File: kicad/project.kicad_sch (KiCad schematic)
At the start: 15 parts, among them IC1A Conn_02x08_Counter_Clockwise, IC1B Conn_02x08_Counter_Clockwise, Q1 AO3402, Q2 AO3401, SW1 RotaryEncoder_Switch, U2 I2C 0.91 OLED

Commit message: Updating the schematic with footprint and symbol
Tiny weaks to pin assignment
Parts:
- removed IC1A, IC1B: Conn_02x08_Counter_Clockwise, symbol Connector_Generic:Conn_02x08_Counter_Clockwise
- added U1: WEMOS_ESP32_S2_Mini, library:WEMOS_S2_mini, symbol library:WEMOS_ESP32_S2_Mini
- BT1: footprint (none) -> Connector_PinHeader_2.54mm:PinHeader_1x02_P2.54mm_Vertical
- R1, R2, R3, R4, R5, R6, R7: footprint (none) -> Resistor_THT:R_Axial_DIN0207_L6.3mm_D2.5mm_P10.16mm_Horizontal
- U2: value I2C 0.91 OLED -> I2C 0.91 128x32 OLED
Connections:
- net +BATT: now also U1.47 (VBUS)
- net BAT_SENSE: now also U1.17 (GPIO17)
- net DISPLAY_PWR: now also U1.37 (GPIO37)
- net ENC1: now also U1.18 (GPIO18)
- net ENC2: now also U1.21 (GPIO21)
- net ENC_BTN: now also U1.16 (GPIO16)
- net GND: now also U1.48 (GND)
- net IR_LED: now also U1.15 (GPIO15)
- net SCL: now also U1.35 (GPIO35)
- net SDA: now also U1.33 (GPIO33)
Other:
- note removed: "I^{2}C OLED DISPLAY 128x32"
- note removed: "WEMOS ESP32-S2-mini"
- moved on the sheet: BT1, D1, Q1, Q2, R1, R2, R3, R4, R5, R6, R7, SW1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

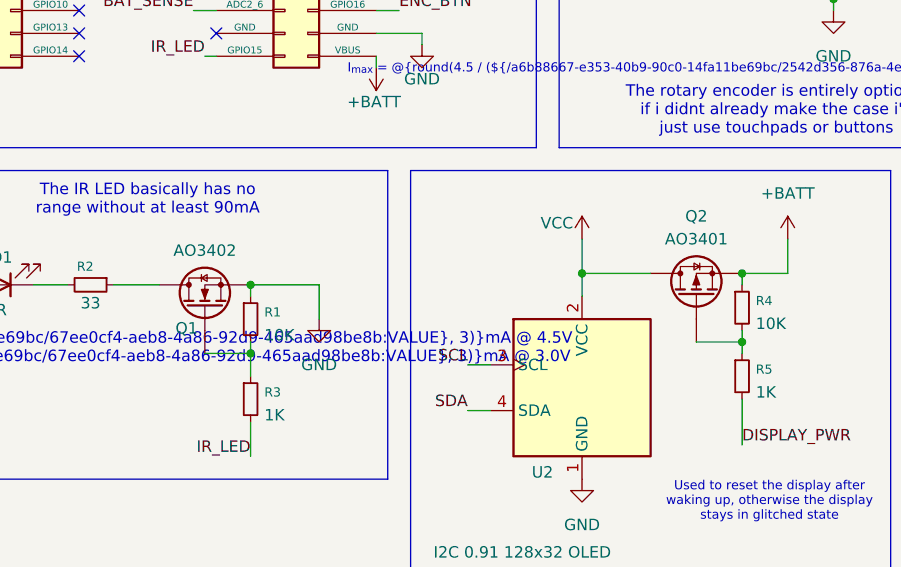
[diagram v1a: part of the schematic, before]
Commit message: Update schematic to show proper pinout of mosfets
As i am soldering this without making a PCB it is very helpful so i dont
have to look at the datasheet all the time
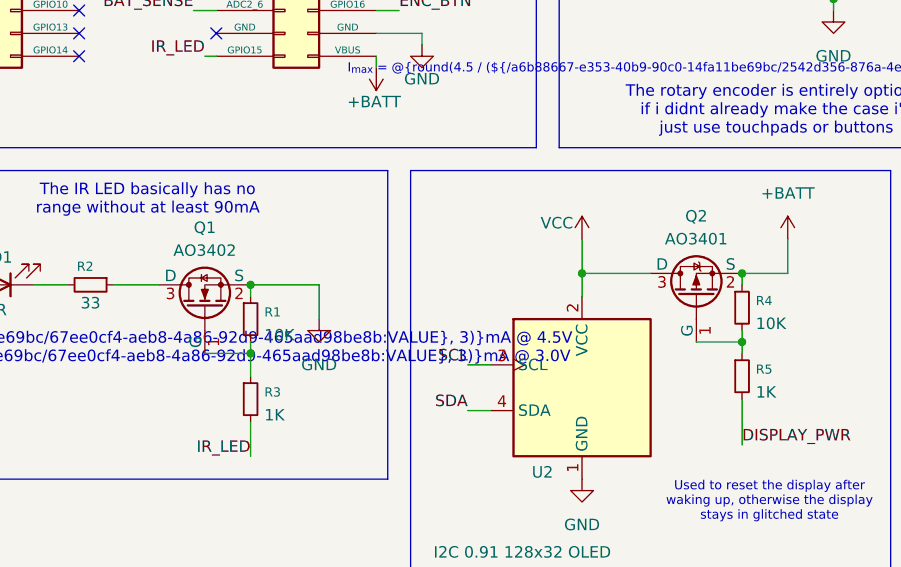
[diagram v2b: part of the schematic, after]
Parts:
- removed Q1: AO3402, Package_TO_SOT_SMD:SOT-23_Handsoldering, symbol Device:Q_NMOS
- removed Q2: AO3401, Package_TO_SOT_SMD:SOT-23_Handsoldering, symbol Device:Q_PMOS
- added Q1: AO3402, Package_TO_SOT_SMD:SOT-23_Handsoldering, symbol library:AO3402
- added Q2: AO3401, Package_TO_SOT_SMD:SOT-23, symbol library:AO3401A
- D1: footprint (none) -> Connector_PinHeader_2.54mm:PinHeader_1x02_P2.54mm_Vertical
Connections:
- net +BATT: now also Q2.2 (S)
- net GND: now also Q1.2 (S)
- net VCC: now also Q2.3 (D)
- net at R1.2, R3.1: now also Q1.1 (G)
- net at R2.1: now also Q1.3 (D)
- net at R4.2, R5.1: now also Q2.1 (G)
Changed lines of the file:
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@@
+	)
+	(junction
+		(at 53.34 64.77)
+		(diameter 0)
+		(color 0 0 0 0)
 	)
 	(junction
@@
 	)
 	(junction
-		(at 53.34 64.77)
-		(diameter 0)
-		(color 0 0 0 0)
-	)
-	(junction
 		(at 53.34 72.39)
 		(diameter 0)
@@
 	)
 	(junction
-		(at 107.95 63.5)
+		(at 118.11 33.02)
 		(diameter 0)
 		(color 0 0 0 0)
 	)
 	(junction
-		(at 118.11 33.02)
+		(at 107.95 63.5)
 		(diameter 0)
 		(color 0 0 0 0)
@@
 			)
 		)
-		(property "Footprint" ""
+		(property "Footprint" "Connector_PinHeader_2.54mm:PinHeader_1x02_P2.54mm_Vertical"
 			(at 25.4 64.77 0)
 			(hide yes)
@@
 	)
 	(symbol
+		(lib_id "library:AO3401A")
+		(at 102.87 66.04 90)
+		(unit 1)
+		(body_style 1)
+		(exclude_from_sim no)
+		(in_bom yes)
+		(on_board yes)
+		(in_pos_files yes)
+		(dnp no)
+		(fields_autoplaced yes)
+		(property "Reference" "Q2"
+			(at 102.87 57.15 90)
+			(show_name no)
+			(do_not_autoplace no)
+			(effects
+				(font
+					(size 1.27 1.27)
+				)
+			)
+		)
+		(property "Value" "AO3401"
+			(at 102.87 59.69 90)
+			(show_name no)
+			(do_not_autoplace no)
+			(effects
+				(font
+					(size 1.27 1.27)
+				)
+			)
+		)
+		(property "Footprint" "Package_TO_SOT_SMD:SOT-23"
+			(at 104.775 60.96 0)
+			(hide yes)
+			(show_name no)
+			(do_not_autoplace no)
+			(effects
+				(font
+					(size 1.27 1.27)
+					(italic yes)
+				)
+				(justify left)
+			)
+		)
+		(property "Datasheet" "http://www.aosmd.com/pdfs/datasheet/AO3401A.pdf"
+			(at 106.68 60.96 0)
+			(hide yes)
+			(show_name no)
+			(do_not_autoplace no)
+			(effects
+				(font
+					(size 1.27 1.27)
+				)
+				(justify left)
+			)
+		)
+		(property "Description" "-4.0A Id, -30V Vds, P-Channel MOSFET, SOT-23"
+			(at 102.87 66.04 0)
+			(hide yes)
+			(show_name no)
+			(do_not_autoplace no)
+			(effects
+				(font
+					(size 1.27 1.27)
+				)
+			)
+		)
+		(pin "1"
+		)
+		(pin "2"
+		)
+		(pin "3"
+		)
+		(instances
+			(project "project"
+				(path "/a6b88667-e353-40b9-90c0-14fa11be69bc"
+					(reference "Q2")
+					(unit 1)
+				)
+			)
+		)
+	)
+	(symbol
 		(lib_id "Device:R_Small")
 		(at 35.56 64.77 270)
@@
 	)
 	(symbol
-		(lib_id "Device:Q_NMOS")
-		(at 48.26 67.31 90)
-		(unit 1)
-		(body_style 1)
-		(exclude_from_sim no)
-		(in_bom yes)
-		(on_board yes)
-		(in_pos_files yes)
-		(dnp no)
-		(property "Reference" "Q1"
-			(at 46.228 69.596 90)
-			(show_name no)
-			(do_not_autoplace no)
-			(effects
-				(font
-					(size 1.27 1.27)
-				)
-			)
-		)
-		(property "Value" "AO3402"
-			(at 48.26 60.96 90)
-			(show_name no)
-			(do_not_autoplace no)
-			(effects
-				(font
-					(size 1.27 1.27)
-				)
-			)
-		)
-		(property "Footprint" "Package_TO_SOT_SMD:SOT-23_Handsoldering"
-			(at 45.72 62.23 0)
-			(hide yes)
-			(show_name no)
-			(do_not_autoplace no)
-			(effects
-				(font
-					(size 1.27 1.27)
-				)
-			)
-		)
-		(property "Datasheet" ""
-			(at 48.26 67.31 0)
-			(hide yes)
-			(show_name no)
-			(do_not_autoplace no)
-			(effects
-				(font
-					(size 1.27 1.27)
-				)
-			)
-		)
-		(property "Description" "N-MOSFET transistor"
-			(at 48.26 67.31 0)
-			(hide yes)
-			(show_name no)
-			(do_not_autoplace no)
-			(effects
-				(font
-					(size 1.27 1.27)
-				)
-			)
-		)
-		(pin "G"
-		)
-		(pin "D"
-		)
-		(pin "S"
-		)
-		(instances
-			(project "project"
-				(path "/a6b88667-e353-40b9-90c0-14fa11be69bc"
-					(reference "Q1")
-					(unit 1)
-				)
-			)
-		)
-	)
-	(symbol
 		(lib_id "Device:R_Small")
 		(at 149.86 30.48 180)
@@
 	)
 	(symbol
-		(lib_id "Device:Q_PMOS")
-		(at 102.87 66.04 90)
+		(lib_id "library:AO3402")
+		(at 48.26 67.31 90)
 		(unit 1)
 		(body_style 1)
@@
 		(dnp no)
 		(fields_autoplaced yes)
-		(property "Reference" "Q2"
-			(at 102.87 57.15 90)
-			(show_name no)
-			(do_not_autoplace no)
-			(effects
-				(font
-					(size 1.27 1.27)
-				)
-			)
-		)
-		(property "Value" "AO3401"
-			(at 102.87 59.69 90)
+		(property "Reference" "Q1"
+			(at 48.26 58.42 90)
+			(show_name no)
+			(do_not_autoplace no)
+			(effects
+				(font
+					(size 1.27 1.27)
+				)
+			)
+		)
+		(property "Value" "AO3402"
+			(at 48.26 60.96 90)
 			(show_name no)
 			(do_not_autoplace no)
@@
 		)
 		(property "Footprint" "Package_TO_SOT_SMD:SOT-23_Handsoldering"
-			(at 100.33 60.96 0)
-			(hide yes)
-			(show_name no)
-			(do_not_autoplace no)
-			(effects
-				(font
-					(size 1.27 1.27)
-				)
-			)
-		)
-		(property "Datasheet" ""
-			(at 102.87 66.04 0)
-			(hide yes)
-			(show_name no)
-			(do_not_autoplace no)
-			(effects
-				(font
-					(size 1.27 1.27)
-				)
-			)
-		)
-		(property "Description" "P-MOSFET transistor"
-			(at 102.87 66.04 0)
-			(hide yes)
-			(show_name no)
-			(do_not_autoplace no)
-			(effects
-				(font
-					(size 1.27 1.27)
-				)
-			)
-		)
-		(pin "G"
-		)
-		(pin "D"
-		)
-		(pin "S"
+			(at 50.165 62.23 0)
+			(hide yes)
+			(show_name no)
+			(do_not_autoplace no)
+			(effects
+				(font
+					(size 1.27 1.27)
+					(italic yes)
+				)
+				(justify left)
+			)
+		)
+		(property "Datasheet" "https://www.sunrom.com/download/504.pdf"
+			(at 52.07 62.23 0)
+			(hide yes)
+			(show_name no)
+			(do_not_autoplace no)
+			(effects
+				(font
+					(size 1.27 1.27)
+				)
+				(justify left)
+			)
+		)
+		(property "Description" "30V Vds, 5.7A Id, N-Channel MOSFET, SOT-23"
+			(at 48.26 67.31 0)
+			(hide yes)
+			(show_name no)
+			(do_not_autoplace no)
+			(effects
+				(font
+					(size 1.27 1.27)
+				)
+			)
+		)
+		(pin "3"
+		)
+		(pin "1"
+		)
+		(pin "2"
 		)
 		(instances
 			(project "project"
 				(path "/a6b88667-e353-40b9-90c0-14fa11be69bc"
-					(reference "Q2")
+					(reference "Q1")
 					(unit 1)
 				)

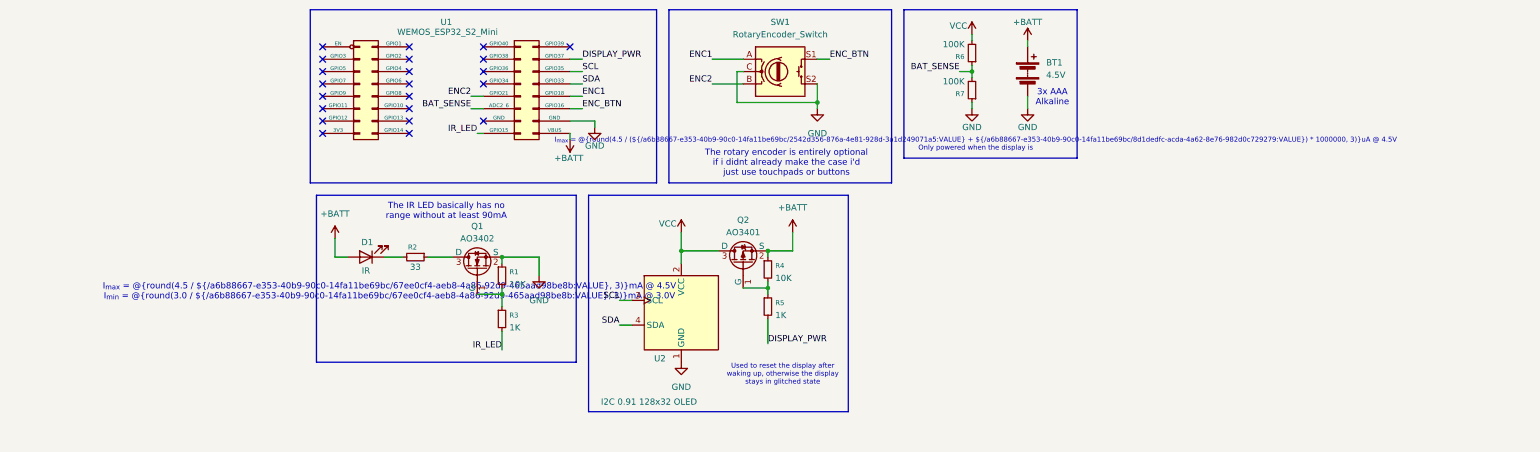
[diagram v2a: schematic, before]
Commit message: Updating the schematic
Im using an NPN transistor to trigger a PMOS which cuts off power to the
OLED screen, also cleaned up the schematic and added pinouts for
transistors
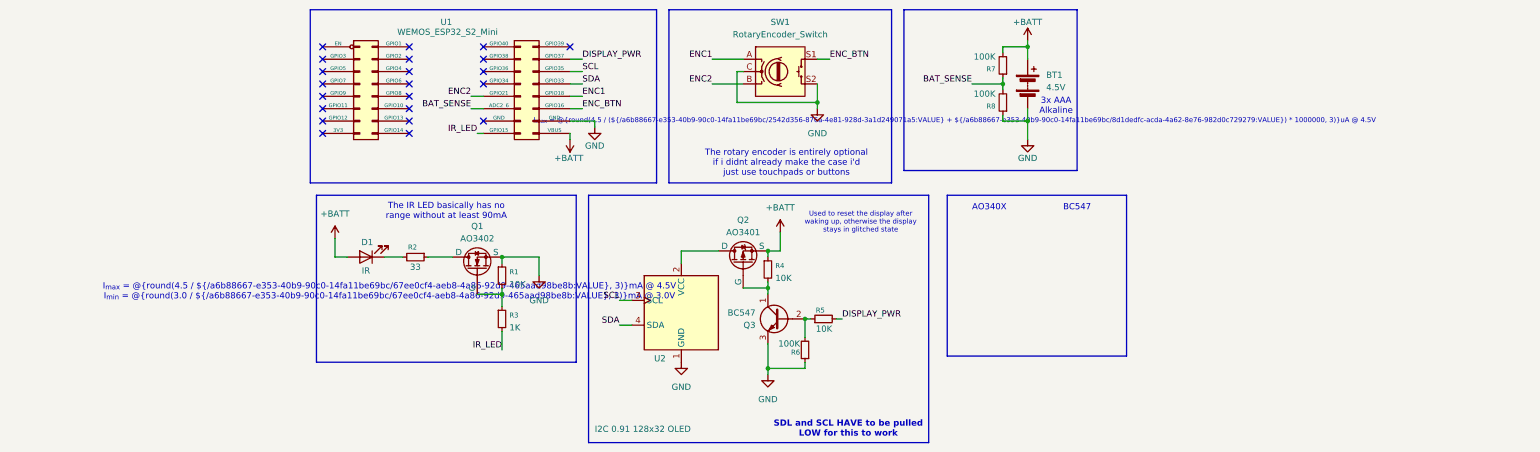
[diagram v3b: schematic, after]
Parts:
- added Q3: BC547, Package_TO_SOT_THT:TO-92_Inline, symbol Transistor_BJT:BC547
- added R6: 100K, Resistor_THT:R_Axial_DIN0207_L6.3mm_D2.5mm_P10.16mm_Horizontal, symbol Device:R_Small
- R5: value 1K -> 10K
- renumbered R6 to R7, R7 to R8
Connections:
- net +BATT: now also R7.2
- net GND: now also Q3.3 (E), R6.1
- net at Q2.1 (G), R4.2: now also Q3.1 (C); no longer R5.1
- net VCC: no longer names the net of Q2.3 (D), U2.2 (VCC)
- net VCC: no longer R7.2
- new net: Q3.2 (B), R5.1, R6.2
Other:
- note added: "AO340X"
- note added: "BC547"
- note added: "I_{max} = @{round(4.5 / (${/a6b88667-e353-40b9-90c0-14fa11be69bc/2542d356-876a-4e81-928d-3a1d249071a5:VALUE} + ${/a6b88667-e353-40b9-90c0-14fa11be69bc/8d1dedfc-acda-4a62-8e76-982d0c729279:VALUE}) * 1000000, 3)}uA @ 4.5V"
- note added: "SDL and SCL HAVE to be pulled LOW for this to work"
- note removed: "I_{max} = @{round(4.5 / (${/a6b88667-e353-40b9-90c0-14fa11be69bc/2542d356-876a-4e81-928d-3a1d249071a5:VALUE} + ${/a6b88667-e353-40b9-90c0-14fa11be69bc/8d1dedfc-acda-4a62-8e76-982d0c729279:VALUE}) * 1000000, 3)}uA @ 4.5V Only powered when the display is"
- moved on the sheet: BT1, R5, R7, R8
